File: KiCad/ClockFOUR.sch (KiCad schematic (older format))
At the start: 68 parts, among them P1 ICSP, P10 Marquee, P2 FTDI, P3 PWR_IN, P5 PWR_IN, P6 5VEN_L, P7 I2C_L, P8 5VEN_R, P9 I2C_R, SW1 SW_RST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

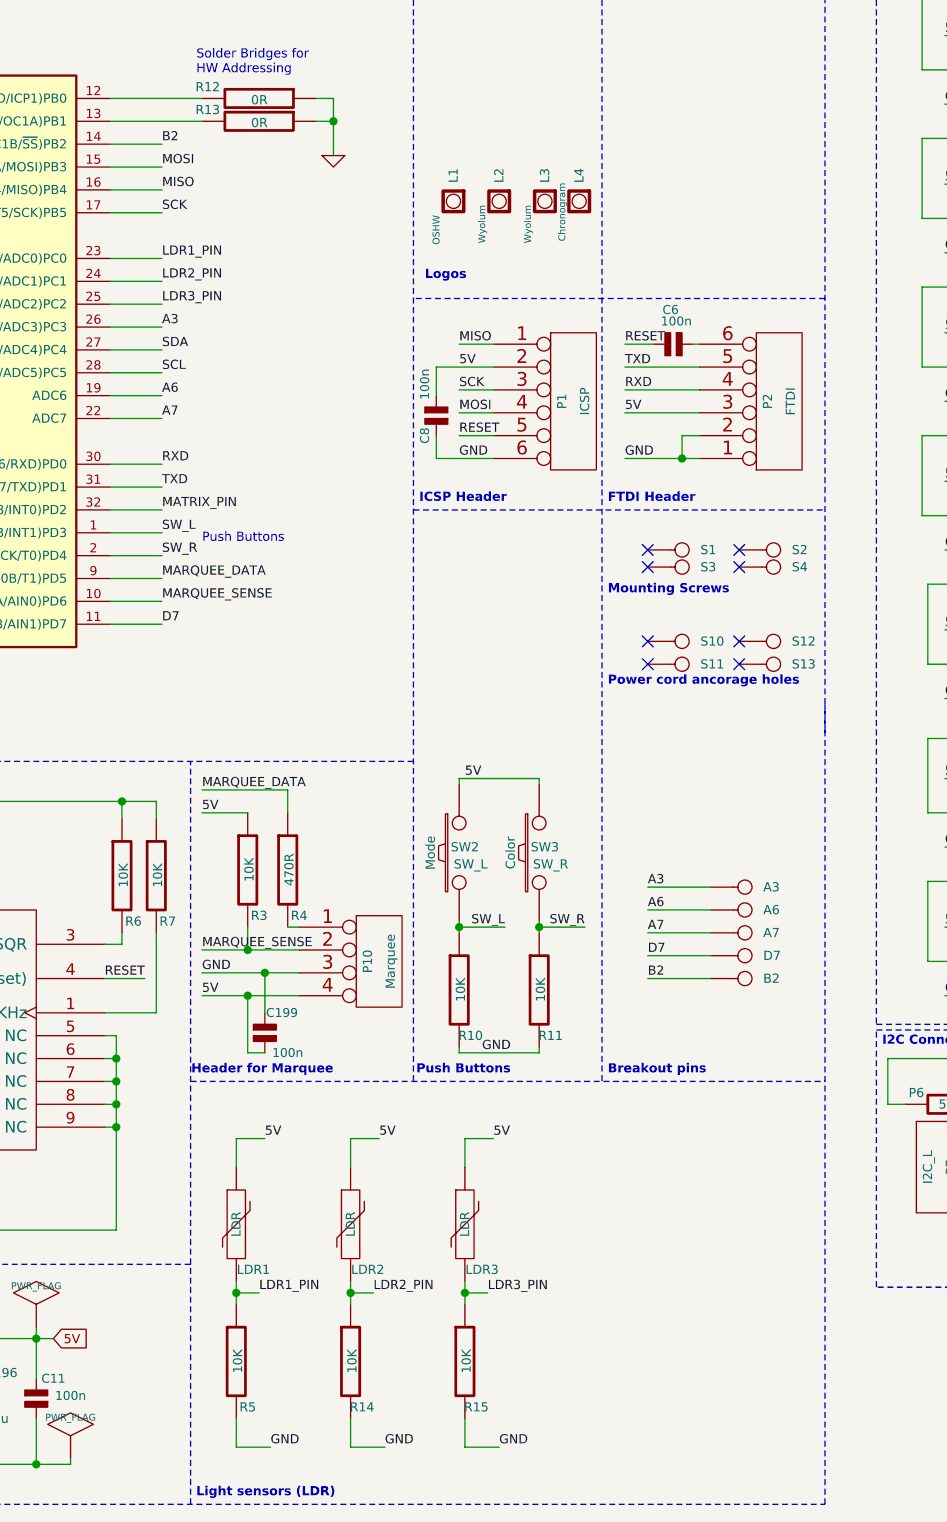
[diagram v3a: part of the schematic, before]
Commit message: added LDR4
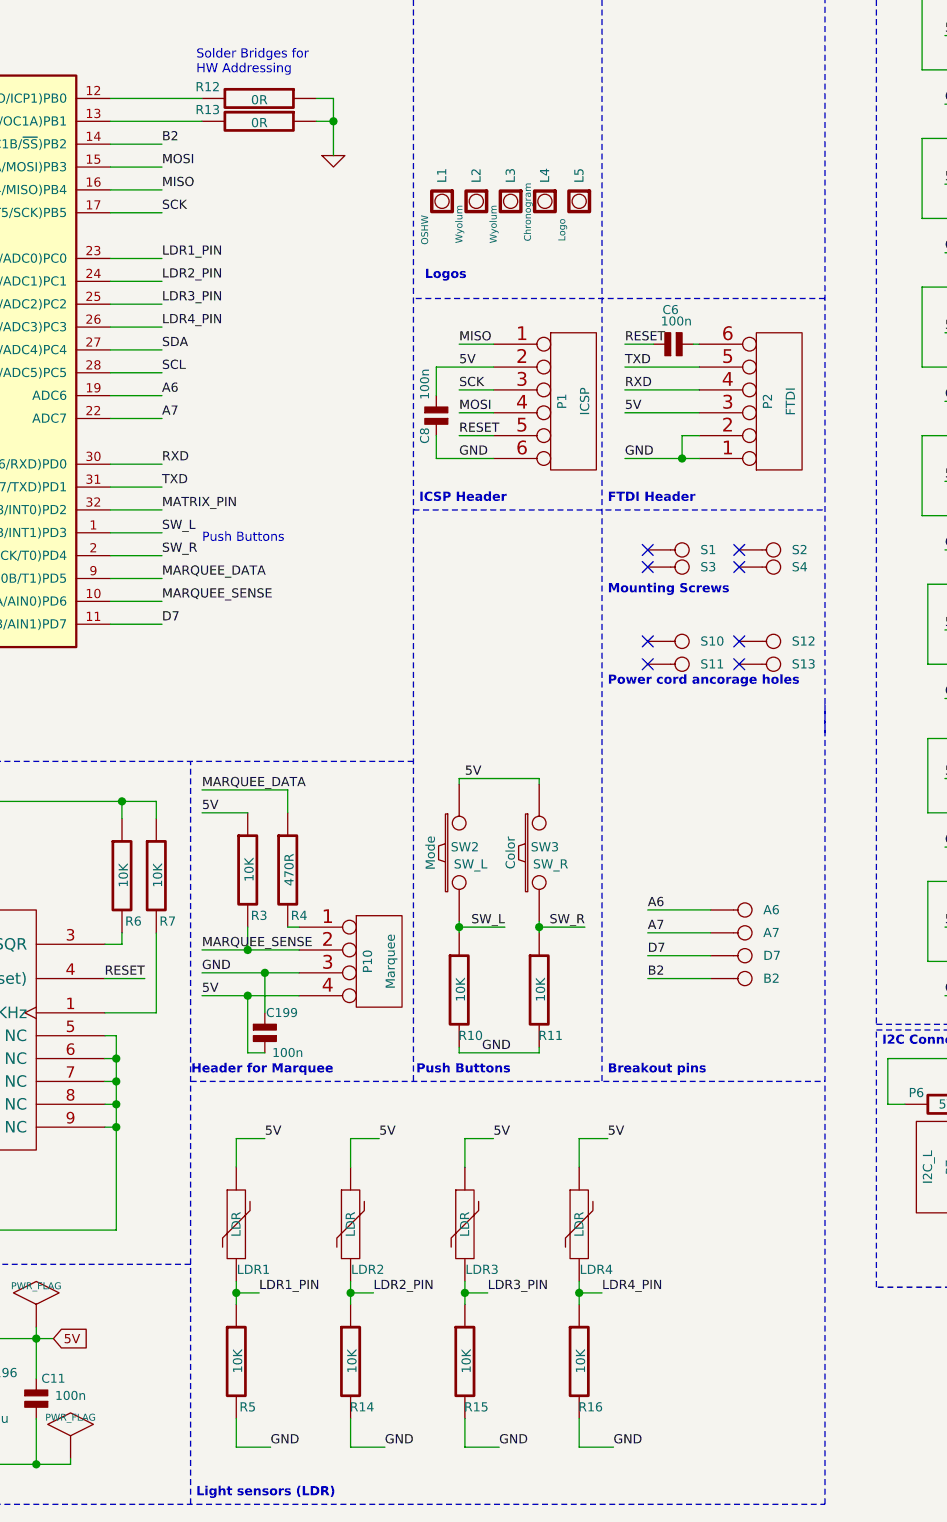
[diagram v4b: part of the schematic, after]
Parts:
- removed A3: CONN_1, C4_Pretty:BreakOutPad, symbol CONN_1
- added L5: Logo, C4_Pretty:Logo_silk_OSHW_6x6mm, symbol Logos
- added LDR4: LDR, C4_Pretty:r_0805_ldr, symbol VR
- added R16: 10K, C4_Pretty:r_0805, symbol R
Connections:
- net GND: now also R16.2
- net VCC: now also LDR4.1
- net A3 renamed LDR4_PIN
- net LDR4_PIN: now also LDR4.2, R16.1
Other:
- moved on the sheet: L1, L2, L3, L4
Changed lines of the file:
@@
 C1 ED 35 72 E0 F7 FB FF F1 1F FF F1 9F FF F9 9F C7 C7 C7 73 1A 9F 2B 70 38 1C FB F6 ED 3B 79 F2
 E4 23 8F 3C 52 B0 F1 D9 2E 76 F1 FF 03 17 ED 19 47 28 92 59 FB 00 00 00 00 49 45 4E 44 AE 42 60
-82 B7
+82 D7
 EndData
 $EndBitmap
@@
 L Logos L1
 U 1 1 511CD9F8
-P 5050 1725
-F 0 "L1" H 5130 1725 40  0000 L CNN
-F 1 "OSHW" H 4925 1800 30  0000 C CNN
-F 2 "C4_Pretty:Logo_silk_OSHW_6x6mm" H 5050 1880 30  0001 C CNN
-F 3 "" H 5050 1725 60  0001 C CNN
-	1    5050 1725
+P 5000 1725
+F 0 "L1" H 5080 1725 40  0000 L CNN
+F 1 "OSHW" H 4875 1800 30  0000 C CNN
+F 2 "C4_Pretty:Logo_silk_OSHW_6x6mm" H 5000 1880 30  0001 C CNN
+F 3 "" H 5000 1725 60  0001 C CNN
+	1    5000 1725
 	0    -1   -1   0
 $EndComp
@@
 L Logos L2
 U 1 1 511CD9F5
-P 5250 1725
-F 0 "L2" H 5330 1725 40  0000 L CNN
-F 1 "Wyolum" H 5150 1800 30  0000 C CNN
-F 2 "C4_Pretty:Logo-WL3" H 5175 1800 30  0001 C CNN
-F 3 "" H 5250 1725 60  0001 C CNN
-	1    5250 1725
+P 5150 1725
+F 0 "L2" H 5230 1725 40  0000 L CNN
+F 1 "Wyolum" H 5050 1800 30  0000 C CNN
+F 2 "C4_Pretty:Logo-WL3" H 5075 1800 30  0001 C CNN
+F 3 "" H 5150 1725 60  0001 C CNN
+	1    5150 1725
 	0    -1   -1   0
 $EndComp
@@
 Text Label 3775 2175 0    40   ~ 0
 LDR3_PIN
-Text Label 3775 2275 0    40   ~ 0
-A3
 Text Notes 725  4125 0    40   ~ 8
 Arduino
@@
 L Logos L3
 U 1 1 5439906B
-P 5450 1725
-F 0 "L3" H 5530 1725 40  0000 L CNN
-F 1 "Wyolum" H 5350 1800 30  0000 C CNN
-F 2 "C4_Pretty:Logo-WL3" H 5375 1800 30  0001 C CNN
-F 3 "" H 5450 1725 60  0001 C CNN
-	1    5450 1725
+P 5300 1725
+F 0 "L3" H 5380 1725 40  0000 L CNN
+F 1 "Wyolum" H 5200 1800 30  0000 C CNN
+F 2 "C4_Pretty:Logo-WL3" H 5225 1800 30  0001 C CNN
+F 3 "" H 5300 1725 60  0001 C CNN
+	1    5300 1725
 	0    -1   -1   0
 $EndComp
@@
 	1    0    0    -1
 $EndComp
-$Comp
-L CONN_1 A3
-U 1 1 54C0C616
-P 6325 4725
-F 0 "A3" H 6405 4725 40  0000 L CNN
-F 1 "CONN_1" H 6325 4780 30  0001 C CNN
-F 2 "C4_Pretty:BreakOutPad" H 6325 4725 60  0001 C CNN
-F 3 "" H 6325 4725 60  0000 C CNN
-	1    6325 4725
-	1    0    0    -1
-$EndComp
-Text Label 5900 4725 0    40   ~ 0
-A3
 Text Label 3950 5000 0    40   ~ 0
 MARQUEE_SENSE
@@
 Wire Wire Line
 	3950 5100 4375 5100
-Wire Wire Line
-	6175 4725 5900 4725
 Wire Wire Line
 	4225 5275 4225 5100
@@
 L Logos L4
 U 1 1 54C81555
-P 5600 1725
-F 0 "L4" H 5680 1725 40  0000 L CNN
-F 1 "Chronogram" H 5425 1800 30  0000 L CNN
-F 2 "C4_Pretty:Logo_silk_OSHW_6x6mm" H 5600 1880 30  0001 C CNN
-F 3 "" H 5600 1725 60  0001 C CNN
-	1    5600 1725
+P 5450 1725
+F 0 "L4" H 5530 1725 40  0000 L CNN
+F 1 "Chronogram" H 5275 1800 30  0000 L CNN
+F 2 "C4_Pretty:Logo_silk_OSHW_6x6mm" H 5450 1880 30  0001 C CNN
+F 3 "" H 5450 1725 60  0001 C CNN
+	1    5450 1725
 	0    -1   -1   0
 $EndComp
@@
 	2250 6775 2250 6700
 Connection ~ 2250 6700
+$Comp
+L VR LDR4
+U 1 1 5610021D
+P 5600 6200
+F 0 "LDR4" H 5675 6025 40  0000 C TNN
+F 1 "LDR" V 5600 6200 40  0000 C CNN
+F 2 "C4_Pretty:r_0805_ldr" H 5600 6200 60  0001 C CNN
+F 3 "~" H 5600 6200 60  0000 C CNN
+	1    5600 6200
+	1    0    0    -1
+$EndComp
+$Comp
+L R R16
+U 1 1 56100223
+P 5600 6800
+F 0 "R16" H 5650 6600 40  0000 C CNN
+F 1 "10K" V 5607 6801 40  0000 C CNN
+F 2 "C4_Pretty:r_0805" V 5530 6800 30  0001 C CNN
+F 3 "~" H 5600 6800 30  0000 C CNN
+	1    5600 6800
+	1    0    0    -1
+$EndComp
+Text Label 5700 6500 0    40   ~ 0
+LDR4_PIN
+Text Label 5725 5825 0    40   ~ 0
+5V
+Text Label 5750 7175 0    40   ~ 0
+GND
+Wire Wire Line
+	5600 5825 5600 5950
+Wire Wire Line
+	5600 6450 5600 6550
+Wire Wire Line
+	5600 7050 5600 7175
+Wire Wire Line
+	5600 6500 5700 6500
+Connection ~ 5600 6500
+Wire Wire Line
+	5600 5825 5725 5825
+Wire Wire Line
+	5600 7175 5750 7175
+Text Label 3775 2275 0    40   ~ 0
+LDR4_PIN
+$Comp
+L Logos L5
+U 1 1 561067AE
+P 5600 1725
+F 0 "L5" H 5680 1725 40  0000 L CNN
+F 1 "Logo" H 5425 1800 30  0000 L CNN
+F 2 "C4_Pretty:Logo_silk_OSHW_6x6mm" H 5600 1880 30  0001 C CNN
+F 3 "" H 5600 1725 60  0001 C CNN
+	1    5600 1725
+	0    -1   -1   0
+$EndComp
 $EndSCHEMATC

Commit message: Kicad mods done. Gerbers, PDF ready
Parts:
- added S5, S6: CONN_1, C4_Pretty:MtgHole_3mm, symbol CONN_1
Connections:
- no-connect marks 9 -> 11
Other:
- note added: "Spare holes"
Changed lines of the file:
@@
 EESchema Schematic File Version 2
 LIBS:ClockFOUR
-LIBS:device
 LIBS:ClockFOUR-cache
 EELAYER 25 0
@@
 Sheet 1 14
 Title "ClockFOUR"
-Date "21/01/2015"
-Rev ""
+Date "2015-10-06"
+Rev "ver 3.0"
 Comp "WyoLum"
 Comment1 "www.wyolum.com"
-Comment2 "David Pincus"
+Comment2 ""
 Comment3 ""
 Comment4 ""
@@
 C1 ED 35 72 E0 F7 FB FF F1 1F FF F1 9F FF F9 9F C7 C7 C7 73 1A 9F 2B 70 38 1C FB F6 ED 3B 79 F2
 E4 23 8F 3C 52 B0 F1 D9 2E 76 F1 FF 03 17 ED 19 47 28 92 59 FB 00 00 00 00 49 45 4E 44 AE 42 60
-82 D7
+82 00
 EndData
 $EndBitmap
@@
 	0    -1   -1   0
 $EndComp
+$Comp
+L CONN_1 S5
+U 1 1 56143684
+P 6050 4050
+F 0 "S5" H 6130 4050 40  0000 L CNN
+F 1 "CONN_1" H 6050 4105 30  0001 C CNN
+F 2 "C4_Pretty:MtgHole_3mm" H 6050 4050 60  0001 C CNN
+F 3 "" H 6050 4050 60  0000 C CNN
+	1    6050 4050
+	1    0    0    -1
+$EndComp
+$Comp
+L CONN_1 S6
+U 1 1 56143690
+P 6450 4050
+F 0 "S6" H 6530 4050 40  0000 L CNN
+F 1 "CONN_1" H 6450 4105 30  0001 C CNN
+F 2 "C4_Pretty:MtgHole_3mm" H 6450 4050 60  0001 C CNN
+F 3 "" H 6450 4050 60  0000 C CNN
+	1    6450 4050
+	1    0    0    -1
+$EndComp
+Text Notes 5725 4250 0    40   ~ 8
+Spare holes
+NoConn ~ 5900 4050
+NoConn ~ 6300 4050
 $EndSCHEMATC

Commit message: ClockFOUR ver 3.0 final schematic, layout, gerber plots and BoM for production
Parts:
- P5: footprint C4_Pretty:Header_3x1_PWR -> C4_Pretty:Pin_Header_Angled_1x03
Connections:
- net GND: no longer P3.1, P5.1
- no-connect marks 11 -> 13
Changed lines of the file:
@@
 C1 ED 35 72 E0 F7 FB FF F1 1F FF F1 9F FF F9 9F C7 C7 C7 73 1A 9F 2B 70 38 1C FB F6 ED 3B 79 F2
 E4 23 8F 3C 52 B0 F1 D9 2E 76 F1 FF 03 17 ED 19 47 28 92 59 FB 00 00 00 00 49 45 4E 44 AE 42 60
-82 00
+82 3D
 EndData
 $EndBitmap
@@
 F 0 "P5" V 1300 6800 40  0000 C CNN
 F 1 "PWR_IN" V 1400 6800 40  0000 C CNN
-F 2 "C4_Pretty:Header_3x1_PWR" H 1350 6650 60  0001 C CNN
+F 2 "C4_Pretty:Pin_Header_Angled_1x03" H 1350 6650 60  0001 C CNN
 F 3 "" H 1350 6650 60  0000 C CNN
 	1    1350 6800
 	-1   0    0    1
 $EndComp
-Wire Wire Line
-	1700 6900 1750 6900
-Connection ~ 1750 6900
 $Comp
 L CONN_3 P3
@@
 Connection ~ 1175 7250
 Wire Wire Line
-	1125 6900 1175 6900
-Connection ~ 1175 6900
-Wire Wire Line
 	1125 6700 1175 6700
 Wire Wire Line
@@
 NoConn ~ 5900 4050
 NoConn ~ 6300 4050
+NoConn ~ 1125 6900
+NoConn ~ 1700 6900
 $EndSCHEMATC
